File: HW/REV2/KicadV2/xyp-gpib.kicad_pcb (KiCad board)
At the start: 2 copper layers, 54 x 15 mm, 25 parts, among them J1 USB_C_Receptacle_USB2.0, SW1 SW_Push, U1 ATmega32U4-MU, Y1 CX2016DB16000D0WZRC1

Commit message: Update to KiCAD 8.0.4 and add Digi-Key part numbers.
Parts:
- C7: value 1u -> 1uF
- GPIB1: value 112-024-113R001 -> 112-024-113L001; footprint gpib:112024113R001 -> ac125a_dtmf:112024113L001
- R7: value 10k -> 5k1
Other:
- board text added: "GPIB1"
- board text added: "UsbGpib"
- board text removed: "GpibUsb"

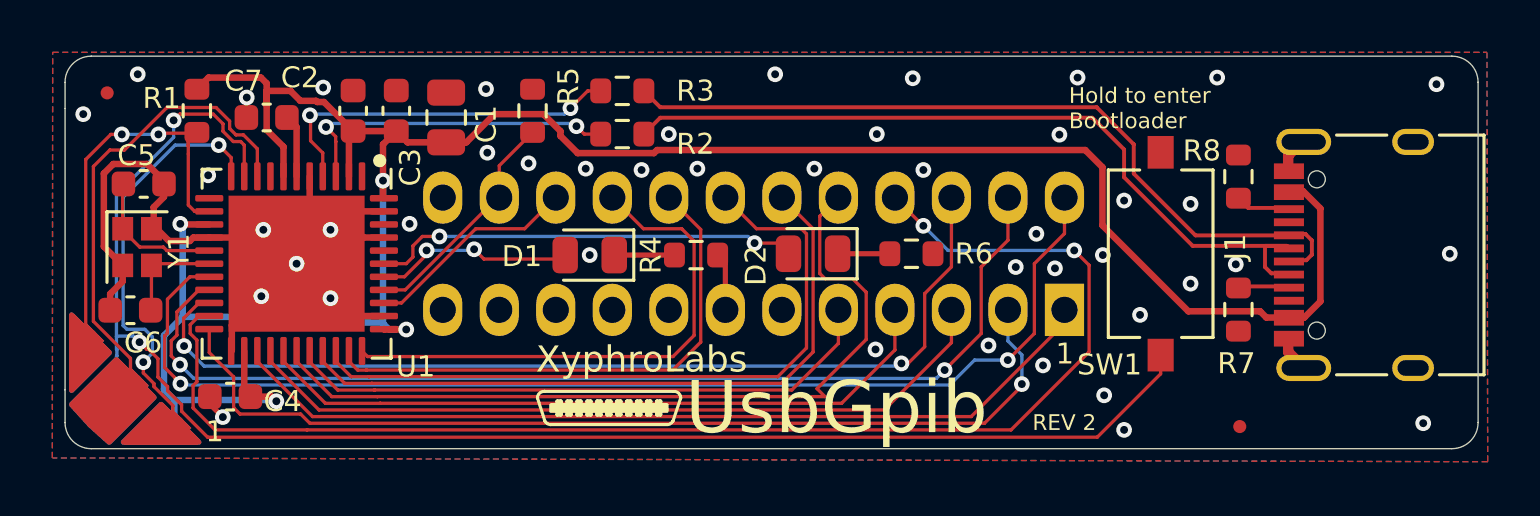
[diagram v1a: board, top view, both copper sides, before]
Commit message: Fix pinout and pin 1 orientation of GPIB connector.
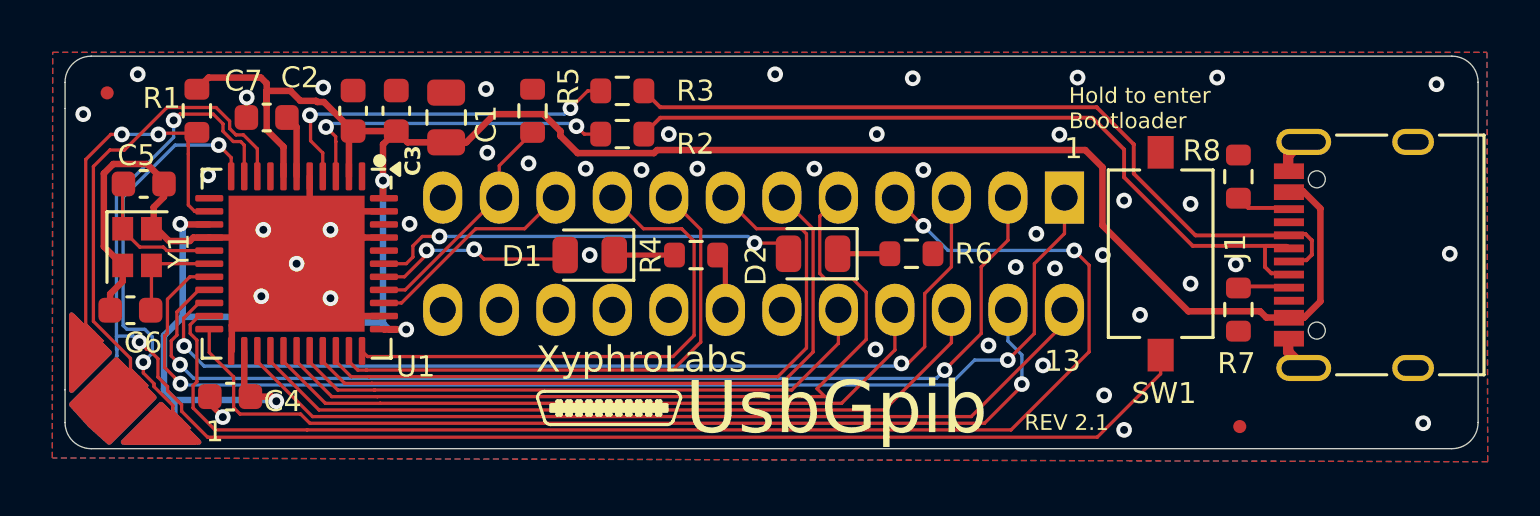
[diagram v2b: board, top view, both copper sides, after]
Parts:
- GPIB1: footprint ac125a_dtmf:112024113L001 -> ac125a_dtmf:111-024-113L001
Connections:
- net Net-(D1-A) renamed /PF5
- net Net-(D2-A) renamed /PF4
- GPIB1 pad 1: /DIO5 -> /DIO1
- GPIB1 pad 10: /EOI -> /SRQ
- GPIB1 pad 11: GND -> /ATN
- GPIB1 pad 12: /DAV -> GND
- GPIB1 pad 13: GND -> /DIO5
- GPIB1 pad 14: /NRFD -> /DIO6
- GPIB1 pad 15: GND -> /DIO7
- GPIB1 pad 16: /NDAC -> /DIO8
- GPIB1 pad 17: GND -> /REN
- GPIB1 pad 18: /IFC -> GND
- GPIB1 pad 2: /DIO1 -> /DIO2
- GPIB1 pad 20: /SRQ -> GND
- GPIB1 pad 22: /ATN -> GND
- GPIB1 pad 3: /DIO6 -> /DIO3
- GPIB1 pad 4: /DIO2 -> /DIO4
- GPIB1 pad 5: /DIO7 -> /EOI
- GPIB1 pad 6: /DIO3 -> /DAV
- GPIB1 pad 7: /DIO8 -> /NRFD
- GPIB1 pad 8: /DIO4 -> /NDAC
- GPIB1 pad 9: /REN -> /IFC
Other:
- board text added: "13"
- board text added: "REV 2.1"
- board text removed: "REV 2"
